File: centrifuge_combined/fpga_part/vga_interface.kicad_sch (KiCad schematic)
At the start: 19 parts, among them J3 Conn_01x15, Q3 BSN20, Q4 BSN20, U13 RCLAMP0524PATCT, U9 LSF0102

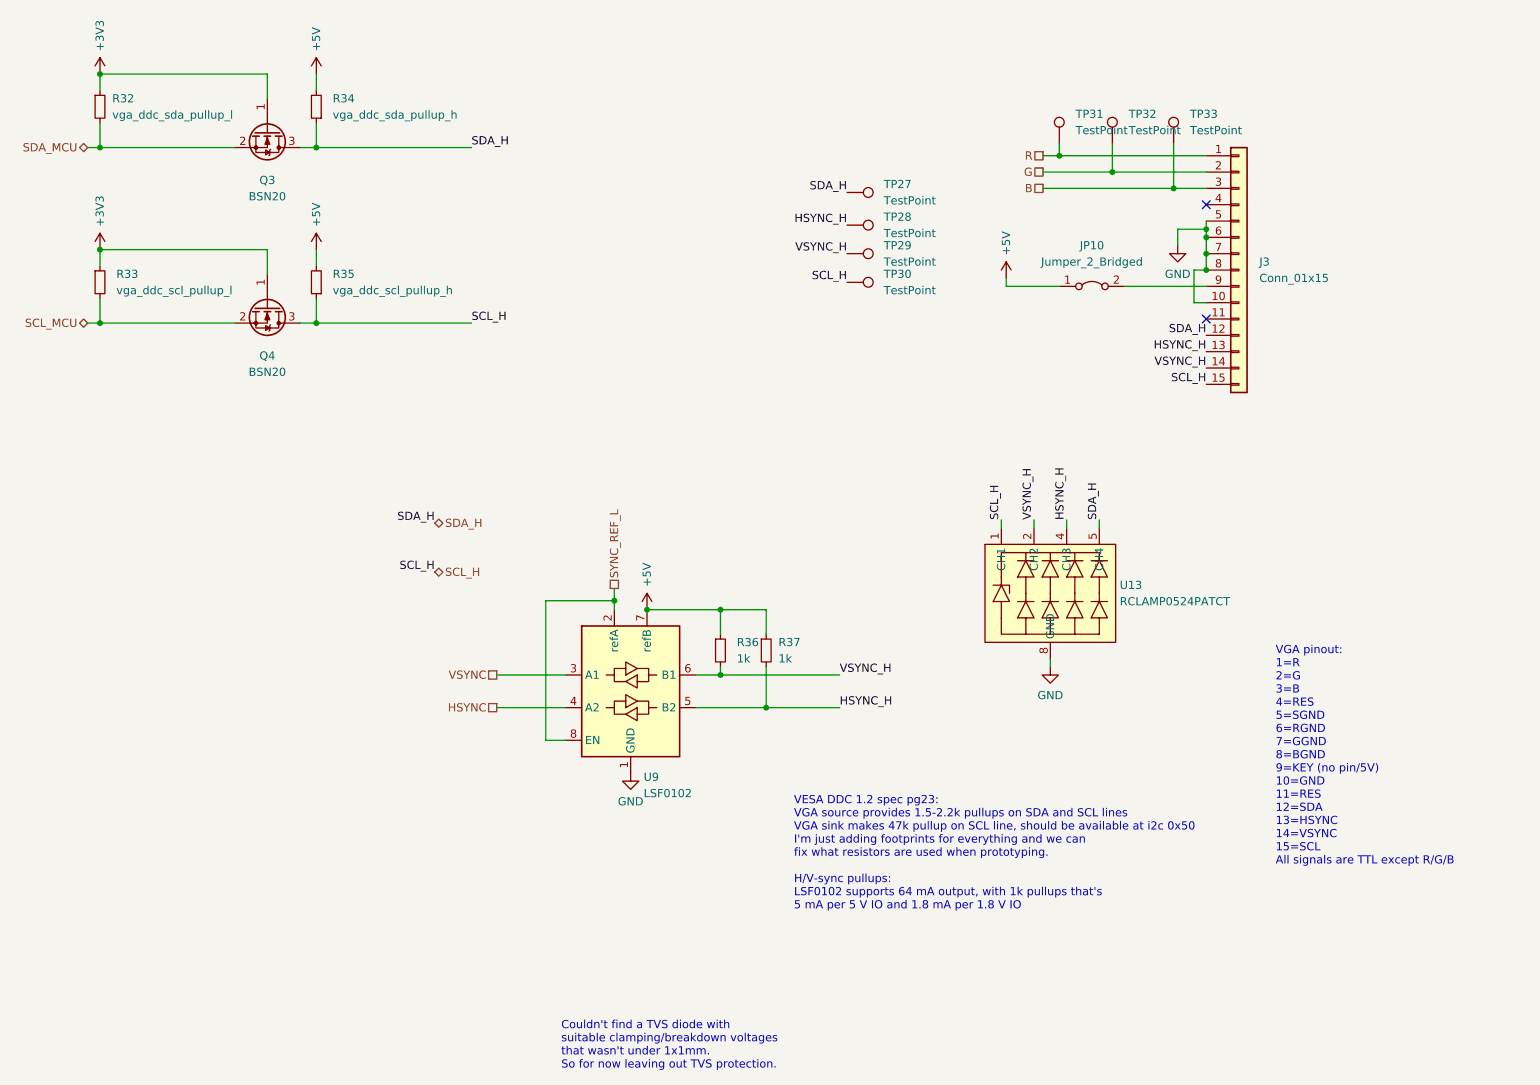
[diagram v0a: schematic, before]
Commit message: change resistor values to have to 2k2, and also make I2C hopefully work
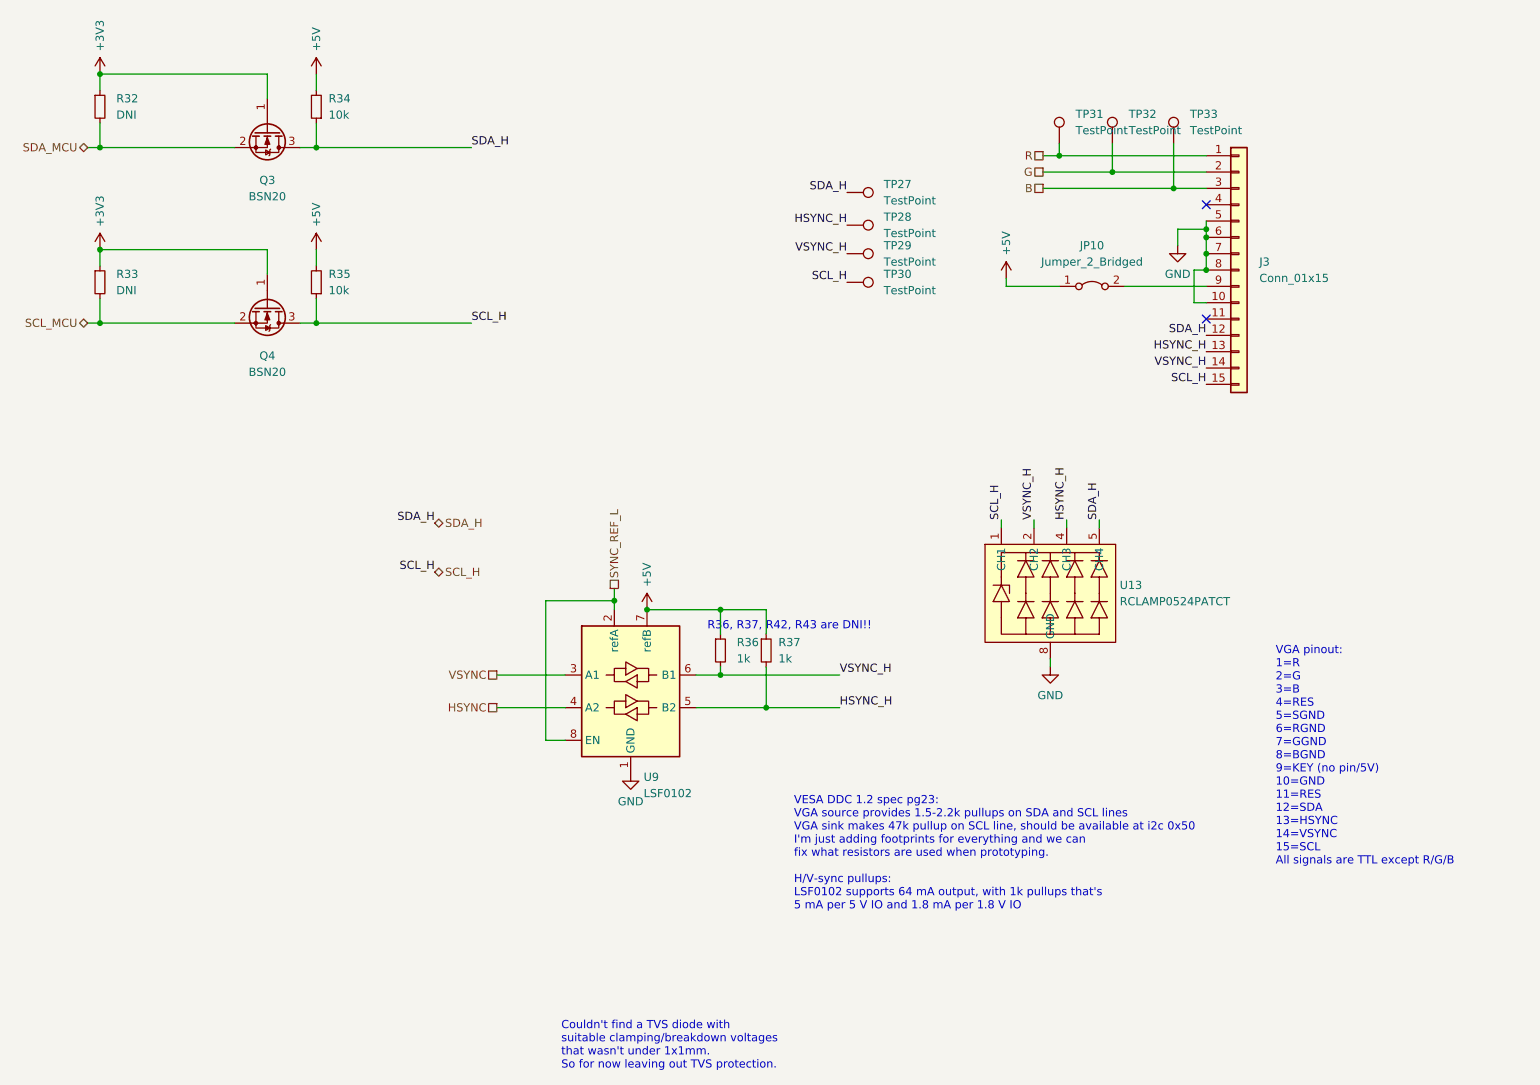
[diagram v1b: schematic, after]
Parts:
- R32: value vga_ddc_sda_pullup_l -> DNI
- R33: value vga_ddc_scl_pullup_l -> DNI
- R34: value vga_ddc_sda_pullup_h -> 10k
- R35: value vga_ddc_scl_pullup_h -> 10k
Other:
- note added: "R36, R37, R42, R43 are DNI!!"
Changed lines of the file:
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@@
+    (effects (font (size 1.27 1.27)) (justify left bottom))
+  )
+  (text "R36, R37, R42, R43 are DNI!!" (at 160.528 120.904 0)
     (effects (font (size 1.27 1.27)) (justify left bottom))
   )
@@
       (effects (font (size 1.27 1.27)) (justify left))
     )
-    (property "Value" "vga_ddc_scl_pullup_l" (id 1) (at 68.58 67.9449 0)
+    (property "Value" "DNI" (id 1) (at 68.58 67.9449 0)
       (effects (font (size 1.27 1.27)) (justify left))
     )
@@
   (symbol (lib_id "Device:R_Small") (at 99.695 66.675 180) (unit 1)
     (in_bom yes) (on_board yes) (fields_autoplaced)
-    (property "Reference" "R35" (id 0) (at 102.235 65.4049 0)
+    (property "Reference" "R35" (id 0) (at 101.6 65.4049 0)
       (effects (font (size 1.27 1.27)) (justify right))
     )
-    (property "Value" "vga_ddc_scl_pullup_h" (id 1) (at 102.235 67.9449 0)
+    (property "Value" "10k" (id 1) (at 101.6 67.9449 0)
       (effects (font (size 1.27 1.27)) (justify right))
     )
@@
   (symbol (lib_id "Device:R_Small") (at 66.04 39.37 0) (unit 1)
     (in_bom yes) (on_board yes) (fields_autoplaced)
-    (property "Reference" "R32" (id 0) (at 67.945 38.0999 0)
-      (effects (font (size 1.27 1.27)) (justify left))
-    )
-    (property "Value" "vga_ddc_sda_pullup_l" (id 1) (at 67.945 40.6399 0)
+    (property "Reference" "R32" (id 0) (at 68.58 38.0999 0)
+      (effects (font (size 1.27 1.27)) (justify left))
+    )
+    (property "Value" "DNI" (id 1) (at 68.58 40.6399 0)
       (effects (font (size 1.27 1.27)) (justify left))
     )
@@
   (symbol (lib_id "Device:R_Small") (at 99.695 39.37 180) (unit 1)
     (in_bom yes) (on_board yes) (fields_autoplaced)
-    (property "Reference" "R34" (id 0) (at 102.235 38.0999 0)
+    (property "Reference" "R34" (id 0) (at 101.6 38.0999 0)
       (effects (font (size 1.27 1.27)) (justify right))
     )
-    (property "Value" "vga_ddc_sda_pullup_h" (id 1) (at 102.235 40.6399 0)
+    (property "Value" "10k" (id 1) (at 101.6 40.6399 0)
       (effects (font (size 1.27 1.27)) (justify right))
     )

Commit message: add note about changes to VGA0's I2C stuff
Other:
- note added: "On the first PCB, in an attempt to make I2C work R12, R13, R14 and R15 are all 4.7k. It didn't work, so now Q1 and Q2 are removed (The 10k's and BSN20's are in their bags)."
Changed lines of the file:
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@@
     (stroke (width 0) (type default) (color 0 0 0 0))
+  )
+  (text "On the first PCB, in an attempt to make I2C work\nR12, R13, R14 and R15 are all 4.7k.\nIt didn't work, so now Q1 and Q2 are removed\n(The 10k's and BSN20's are in their bags)."
+    (at 104.902 56.134 0)
+    (effects (font (size 1.27 1.27)) (justify left bottom))
   )
   (text "Couldn't find a TVS diode with\nsuitable clamping/breakdown voltages\nthat wasn't under 1x1mm.\nSo for now leaving out TVS protection."
